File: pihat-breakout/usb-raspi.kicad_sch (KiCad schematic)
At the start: 19 parts, among them J7 USB_A, U3 TPS259535DSGT

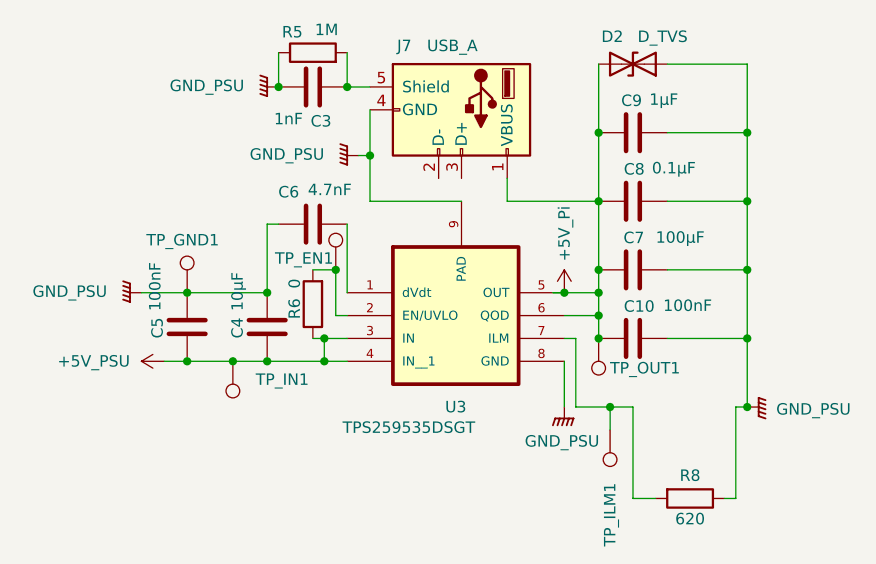
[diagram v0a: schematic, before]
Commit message: fix(0.1uF->100nF)
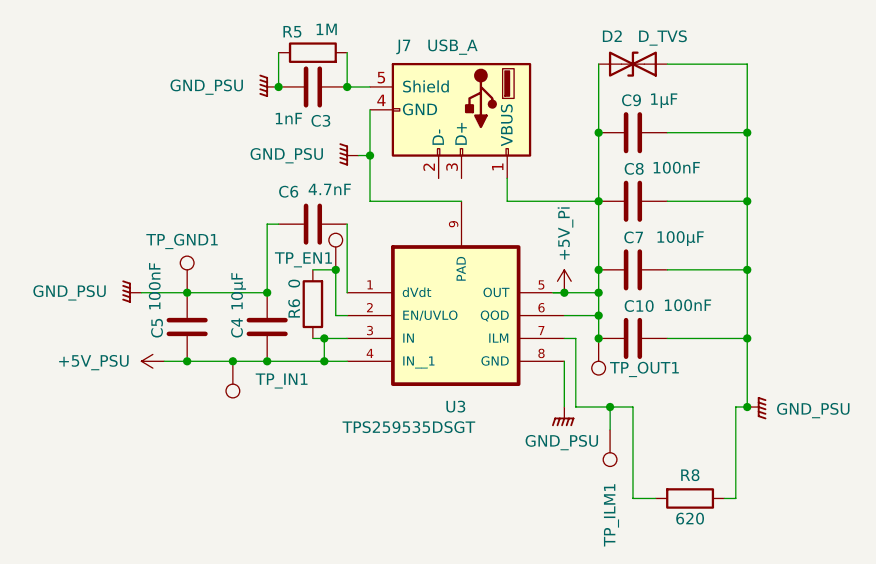
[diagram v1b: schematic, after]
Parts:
- C8: value 0.1µF -> 100nF
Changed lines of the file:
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@@
 			)
 		)
-		(property "Value" "0.1µF"
+		(property "Value" "100nF"
 			(at 176.0973 85.2156 90)
 			(effects
